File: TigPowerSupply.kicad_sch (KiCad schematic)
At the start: 10 parts, among them J1 Screw_Terminal_01x02, J2 Conn_01x03, U1 MCP1826S

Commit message: bla
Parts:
- H1, H2, H3, H4: footprint MountingHole:MountingHole_2.2mm_M2_DIN965 -> MountingHole:MountingHole_3.2mm_M3_DIN965
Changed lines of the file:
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@@
 			)
 		)
-		(property "Footprint" "MountingHole:MountingHole_2.2mm_M2_DIN965"
+		(property "Footprint" "MountingHole:MountingHole_3.2mm_M3_DIN965"
 			(at 90.17 71.12 0)
 			(effects
@@
 			)
 		)
-		(property "Footprint" "MountingHole:MountingHole_2.2mm_M2_DIN965"
+		(property "Footprint" "MountingHole:MountingHole_3.2mm_M3_DIN965"
 			(at 91.44 64.77 0)
 			(effects
@@
 			)
 		)
-		(property "Footprint" "MountingHole:MountingHole_2.2mm_M2_DIN965"
+		(property "Footprint" "MountingHole:MountingHole_3.2mm_M3_DIN965"
 			(at 80.01 71.12 0)
 			(effects
@@
 			)
 		)
-		(property "Footprint" "MountingHole:MountingHole_2.2mm_M2_DIN965"
+		(property "Footprint" "MountingHole:MountingHole_3.2mm_M3_DIN965"
 			(at 80.01 64.77 0)
 			(effects

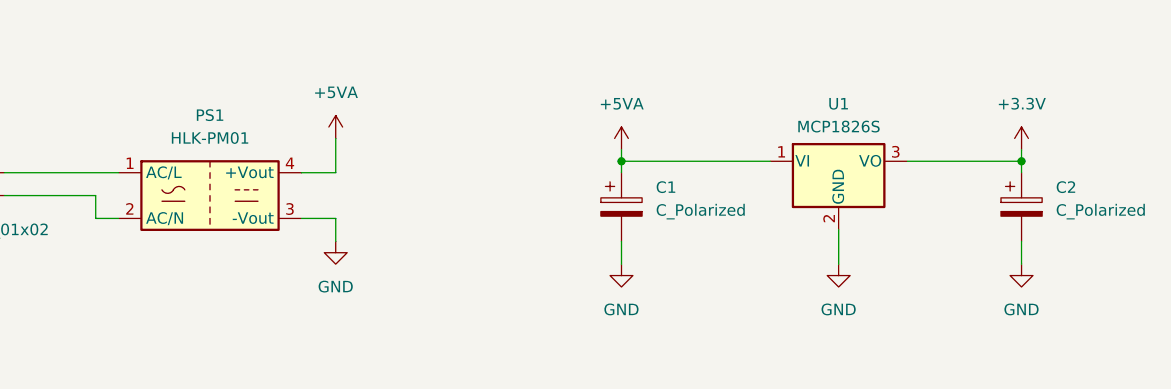
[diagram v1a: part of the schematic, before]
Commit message: moved regulator and changed output connector
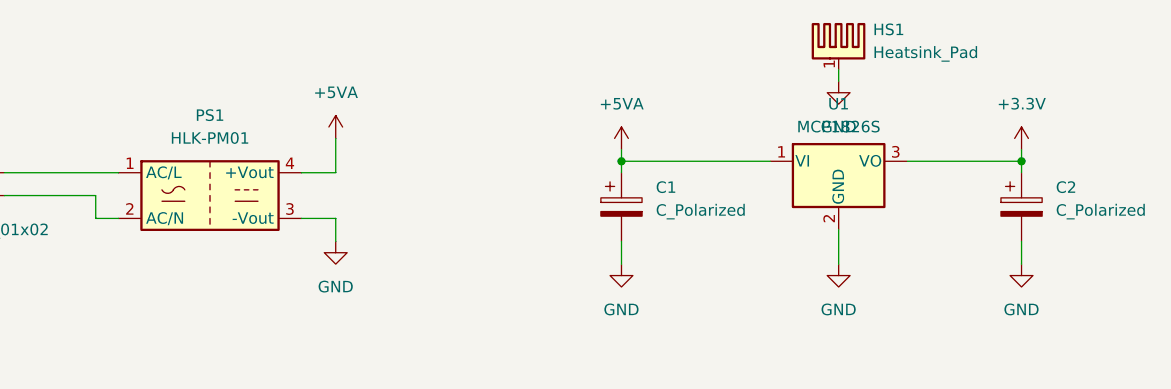
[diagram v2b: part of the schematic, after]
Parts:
- added HS1: Heatsink_Pad, GJ_HeatSink:Heatsink_10x15x40_TTO220, symbol Mechanical:Heatsink_Pad
- J2: footprint Connector_JST:JST_NV_B03P-NV_1x03_P5.00mm_Vertical -> Connector_JST:JST_PH_B3B-PH-K_1x03_P2.00mm_Vertical
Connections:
- net GND: now also HS1.1
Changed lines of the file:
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@@
 (kicad_sch
-	(version 20231120)
+	(version 20250114)
 	(generator "eeschema")
-	(generator_version "8.0")
+	(generator_version "9.0")
 	(paper "A4")
 	(junction
@@
 	(wire
 		(pts
+			(xy 154.94 21.59) (xy 154.94 22.86)
+		)
+		(stroke
+			(width 0)
+			(type default)
+		)
+	)
+	(wire
+		(pts
 			(xy 99.06 29.21) (xy 99.06 33.02)
 		)
@@
 			)
 		)
-		(property "Footprint" "Connector_JST:JST_NV_B03P-NV_1x03_P5.00mm_Vertical"
+		(property "Footprint" "Connector_JST:JST_PH_B3B-PH-K_1x03_P2.00mm_Vertical"
 			(at 233.68 39.37 0)
 			(effects
@@
 	)
 	(symbol
+		(lib_id "Mechanical:Heatsink_Pad")
+		(at 154.94 19.05 0)
+		(unit 1)
+		(exclude_from_sim no)
+		(in_bom yes)
+		(on_board yes)
+		(dnp no)
+		(fields_autoplaced yes)
+		(property "Reference" "HS1"
+			(at 158.75 17.1449 0)
+			(effects
+				(font
+					(size 1.27 1.27)
+				)
+				(justify left)
+			)
+		)
+		(property "Value" "Heatsink_Pad"
+			(at 158.75 19.6849 0)
+			(effects
+				(font
+					(size 1.27 1.27)
+				)
+				(justify left)
+			)
+		)
+		(property "Footprint" "GJ_HeatSink:Heatsink_10x15x40_TTO220"
+			(at 155.2448 20.32 0)
+			(effects
+				(font
+					(size 1.27 1.27)
+				)
+				(hide yes)
+			)
+		)
+		(property "Datasheet" "~"
+			(at 155.2448 20.32 0)
+			(effects
+				(font
+					(size 1.27 1.27)
+				)
+				(hide yes)
+			)
+		)
+		(property "Description" "Heatsink with electrical connection, 1 pin"
+			(at 154.94 19.05 0)
+			(effects
+				(font
+					(size 1.27 1.27)
+				)
+				(hide yes)
+			)
+		)
+		(pin "1"
+		)
+		(instances
+			(project ""
+				(path "/7f75b0e1-4dce-45d1-a236-fcdf5dce52cf"
+					(reference "HS1")
+					(unit 1)
+				)
+			)
+		)
+	)
+	(symbol
 		(lib_id "power:+5VA")
 		(at 99.06 29.21 0)
@@
 				(path "/7f75b0e1-4dce-45d1-a236-fcdf5dce52cf"
 					(reference "H2")
+					(unit 1)
+				)
+			)
+		)
+	)
+	(symbol
+		(lib_id "power:GND")
+		(at 154.94 22.86 0)
+		(unit 1)
+		(exclude_from_sim no)
+		(in_bom yes)
+		(on_board yes)
+		(dnp no)
+		(fields_autoplaced yes)
+		(property "Reference" "#PWR012"
+			(at 154.94 29.21 0)
+			(effects
+				(font
+					(size 1.27 1.27)
+				)
+				(hide yes)
+			)
+		)
+		(property "Value" "GND"
+			(at 154.94 27.94 0)
+			(effects
+				(font
+					(size 1.27 1.27)
+				)
+			)
+		)
+		(property "Footprint" ""
+			(at 154.94 22.86 0)
+			(effects
+				(font
+					(size 1.27 1.27)
+				)
+				(hide yes)
+			)
+		)
+		(property "Datasheet" ""
+			(at 154.94 22.86 0)
+			(effects
+				(font
+					(size 1.27 1.27)
+				)
+				(hide yes)
+			)
+		)
+		(property "Description" "Power symbol creates a global label with name \"GND\" , ground"
+			(at 154.94 22.86 0)
+			(effects
+				(font
+					(size 1.27 1.27)
+				)
+				(hide yes)
+			)
+		)
+		(pin "1"
+		)
+		(instances
+			(project "TigPowerSupply"
+				(path "/7f75b0e1-4dce-45d1-a236-fcdf5dce52cf"
+					(reference "#PWR012")
 					(unit 1)
 				)
@@
 		)
 	)
+	(embedded_fonts no)
 )
